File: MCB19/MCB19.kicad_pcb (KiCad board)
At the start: 2 copper layers, 204 x 81.5 mm, 99 parts, among them J401 USART, J402 DISABLE, J601 RJ45, J602 RJ45, J611 +BAT_IN, J612 -BAT_IN, J613 +BAT_OUT, J614 -BAT_OUT, Q601 IRFP260N, Q602 IRFP260N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

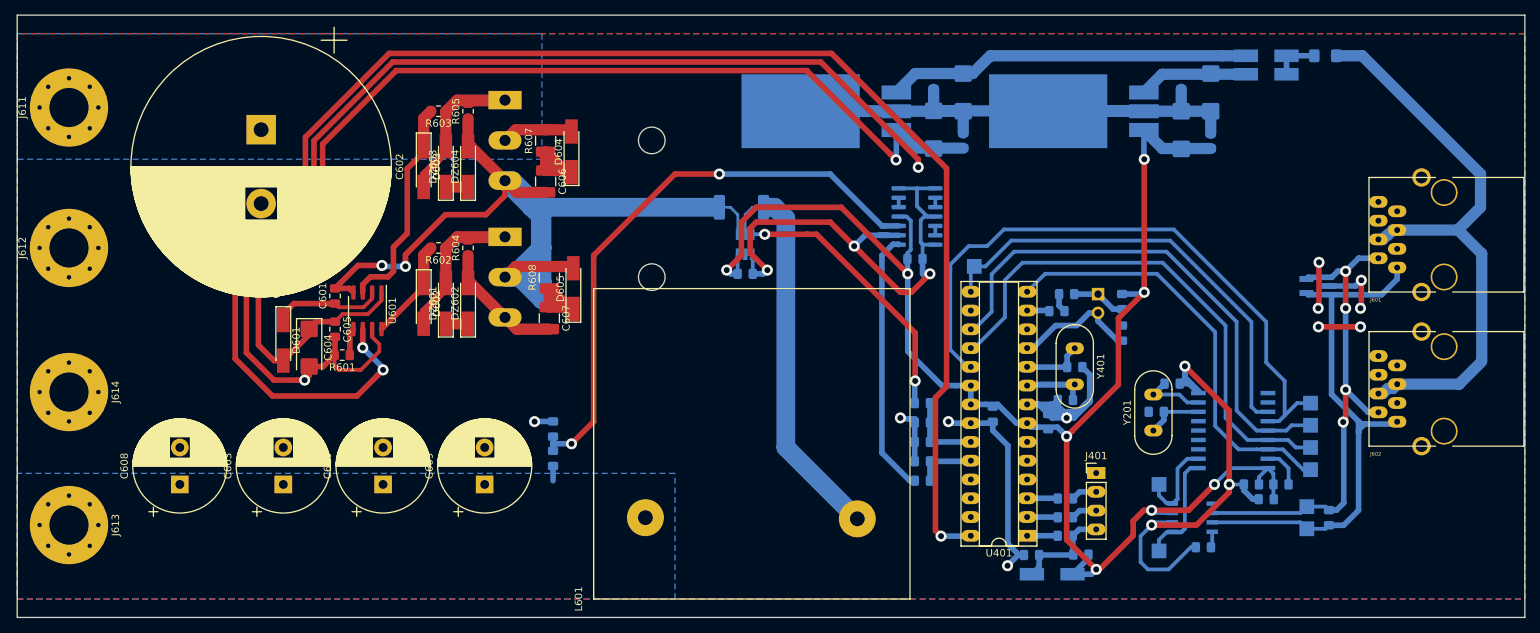
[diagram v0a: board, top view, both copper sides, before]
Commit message: trilhas aumentadas para 30mils
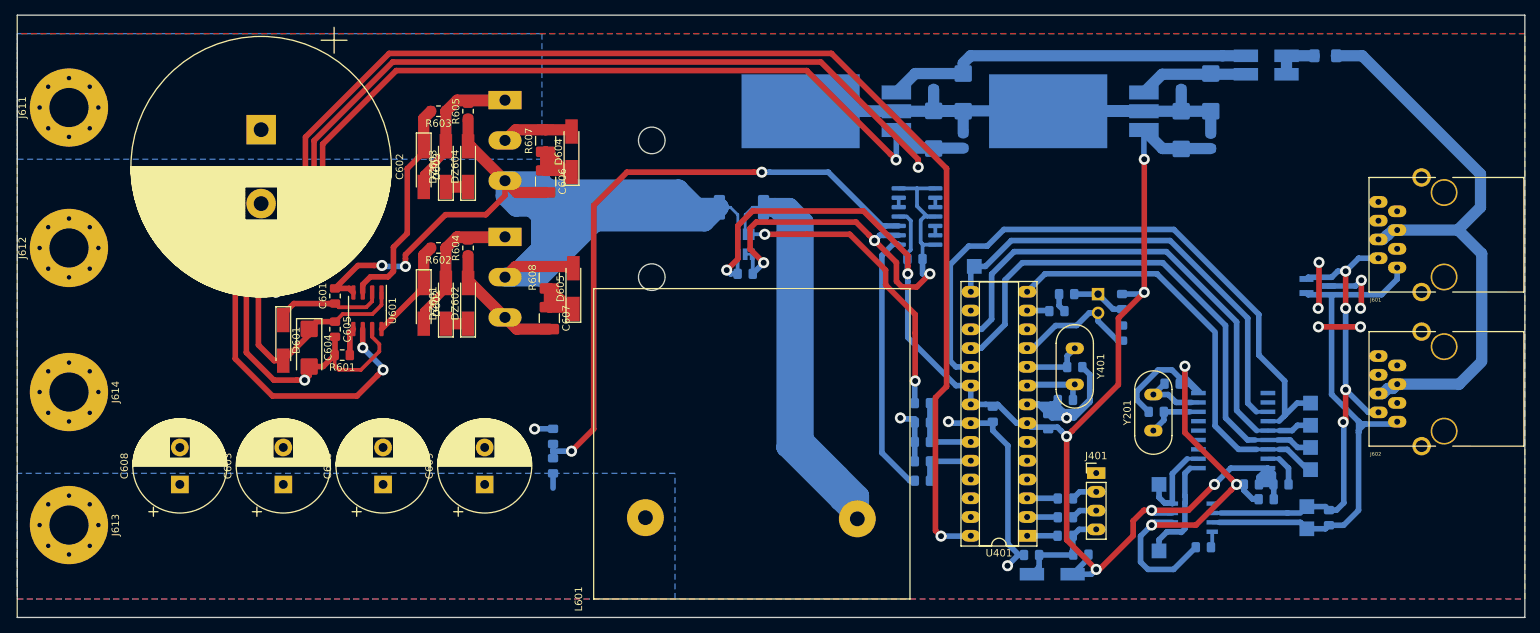
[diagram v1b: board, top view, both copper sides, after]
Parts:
- moved R609 1.00 mm to (122.5, 107.5)
- moved R610 1.00 mm to (122.5, 111.5)
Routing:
- net Net-(C601-Pad2): track 145.5 -> 238.5 mm
- net Net-(L601-Pad2): track 53.3 -> 124.5 mm
- net GND: track 545.9 -> 554.0 mm
- net +5V: track 212.2 -> 217.7 mm
- net Net-(R609-Pad2): track 82.2 -> 87.3 mm
- net /CANBUS/TXCAN: track 17.1 -> 21.7 mm
- net /MCU/INALLL: track 38.8 -> 41.4 mm
- net /SCK: track 86.3 -> 88.3 mm
- net Net-(C501-Pad1): track 49.4 -> 50.2 mm
- net /MOSI: track 70.7 -> 71.3 mm
- net /MISO: track 71.4 -> 71.9 mm

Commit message: 3D added
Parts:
- J402: moved to F.Cu
- moved J402 0.25 mm to (196.0, 88.2), turned to 0 degrees
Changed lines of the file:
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@@
     (visible_elements 7FFFFFFF)
     (pcbplotparams
-      (layerselection 0x00000_fffffffe)
+      (layerselection 0x3ffff_ffffffff)
       (usegerberextensions false)
       (usegerberattributes false)
@@
       (outputformat 4)
       (mirror false)
-      (drillshape 2)
+      (drillshape 0)
       (scaleselection 1)
-      (outputdirectory "GERBERS"))
+      (outputdirectory "PDF"))
   )
   (net 0 "")
@@
     (pad 3 thru_hole oval (at 10.9 0 270) (size 2.5 4.5) (drill 1.5) (layers *.Cu *.Mask)
       (net 37 "Net-(C601-Pad2)"))
-    (model ${KISYS3DMOD}/Package_TO_SOT_THT.3dshapes/TO-247-3_Horizontal_TabUp.wrl
-      (at (xyz 0 0 0))
+    (model "/home/joaoantoniocardoso/ZeniteSolar/2018/MCC18/Hardware/Shunt_sensor/Cuk_converter/KiCad/MCC_bibliotecas/MCCplaca.pretty/3D/User Library-TO-247H.step"
+      (offset (xyz 5.588 -19.558 3.048))
       (scale (xyz 1 1 1))
-      (rotate (xyz 0 0 0))
+      (rotate (xyz 90 0 0))
     )
   )
@@
     (pad 3 thru_hole oval (at 10.9 0 270) (size 2.5 4.5) (drill 1.5) (layers *.Cu *.Mask)
       (net 1 GND))
-    (model ${KISYS3DMOD}/Package_TO_SOT_THT.3dshapes/TO-247-3_Horizontal_TabUp.wrl
-      (at (xyz 0 0 0))
+    (model "/home/joaoantoniocardoso/ZeniteSolar/2018/MCC18/Hardware/Shunt_sensor/Cuk_converter/KiCad/MCC_bibliotecas/MCCplaca.pretty/3D/User Library-TO-247H.step"
+      (offset (xyz 5.588 -19.558 3.048))
       (scale (xyz 1 1 1))
-      (rotate (xyz 0 0 0))
+      (rotate (xyz 90 0 0))
     )
   )
@@
     )
   )
-  (module Connector_PinSocket_2.54mm:PinSocket_1x02_P2.54mm_Vertical (layer B.Cu)
-    (at 196.25 88.25 180)
+  (module Connector_PinSocket_2.54mm:PinSocket_1x02_P2.54mm_Vertical (layer F.Cu)
+    (at 196 88.25)
     (descr "Through hole straight socket strip, 1x02, 2.54mm pitch, single row (from Kicad 4.0.7), script generated")
     (tags "Through hole socket strip THT 1x02 2.54mm single row")
-    (fp_text reference J402 (at 0 2.77 180) (layer B.SilkS)
-      (effects (font (size 1 1) (thickness 0.15)) (justify mirror))
+    (fp_text reference J402 (at 0 -2.77 180) (layer F.SilkS)
+      (effects (font (size 1 1) (thickness 0.15)))
     )
-    (fp_text value DISABLE (at 0 -5.31 180) (layer B.Fab)
-      (effects (font (size 1 1) (thickness 0.15)) (justify mirror))
+    (fp_text value DISABLE (at 0 5.31 180) (layer F.Fab)
+      (effects (font (size 1 1) (thickness 0.15)))
     )
-    (fp_line (start -1.27 1.27) (end 0.635 1.27) (layer B.Fab) (width 0.1))
-    (fp_line (start 0.635 1.27) (end 1.27 0.635) (layer B.Fab) (width 0.1))
-    (fp_line (start 1.27 0.635) (end 1.27 -3.81) (layer B.Fab) (width 0.1))
-    (fp_line (start 1.27 -3.81) (end -1.27 -3.81) (layer B.Fab) (width 0.1))
-    (fp_line (start -1.27 -3.81) (end -1.27 1.27) (layer B.Fab) (width 0.1))
-    (fp_line (start -1.33 -1.27) (end 1.33 -1.27) (layer B.SilkS) (width 0.12))
-    (fp_line (start -1.33 -1.27) (end -1.33 -3.87) (layer B.SilkS) (width 0.12))
-    (fp_line (start -1.33 -3.87) (end 1.33 -3.87) (layer B.SilkS) (width 0.12))
-    (fp_line (start 1.33 -1.27) (end 1.33 -3.87) (layer B.SilkS) (width 0.12))
-    (fp_line (start 1.33 1.33) (end 1.33 0) (layer B.SilkS) (width 0.12))
-    (fp_line (start 0 1.33) (end 1.33 1.33) (layer B.SilkS) (width 0.12))
-    (fp_line (start -1.8 1.8) (end 1.75 1.8) (layer B.CrtYd) (width 0.05))
-    (fp_line (start 1.75 1.8) (end 1.75 -4.3) (layer B.CrtYd) (width 0.05))
-    (fp_line (start 1.75 -4.3) (end -1.8 -4.3) (layer B.CrtYd) (width 0.05))
-    (fp_line (start -1.8 -4.3) (end -1.8 1.8) (layer B.CrtYd) (width 0.05))
-    (fp_text user %R (at 0 -1.27 270) (layer B.Fab)
-      (effects (font (size 1 1) (thickness 0.15)) (justify mirror))
+    (fp_line (start -1.27 -1.27) (end 0.635 -1.27) (layer F.Fab) (width 0.1))
+    (fp_line (start 0.635 -1.27) (end 1.27 -0.635) (layer F.Fab) (width 0.1))
+    (fp_line (start 1.27 -0.635) (end 1.27 3.81) (layer F.Fab) (width 0.1))
+    (fp_line (start 1.27 3.81) (end -1.27 3.81) (layer F.Fab) (width 0.1))
+    (fp_line (start -1.27 3.81) (end -1.27 -1.27) (layer F.Fab) (width 0.1))
+    (fp_line (start -1.33 1.27) (end 1.33 1.27) (layer F.SilkS) (width 0.12))
+    (fp_line (start -1.33 1.27) (end -1.33 3.87) (layer F.SilkS) (width 0.12))
+    (fp_line (start -1.33 3.87) (end 1.33 3.87) (layer F.SilkS) (width 0.12))
+    (fp_line (start 1.33 1.27) (end 1.33 3.87) (layer F.SilkS) (width 0.12))
+    (fp_line (start 1.33 -1.33) (end 1.33 0) (layer F.SilkS) (width 0.12))
+    (fp_line (start 0 -1.33) (end 1.33 -1.33) (layer F.SilkS) (width 0.12))
+    (fp_line (start -1.8 -1.8) (end 1.75 -1.8) (layer F.CrtYd) (width 0.05))
+    (fp_line (start 1.75 -1.8) (end 1.75 4.3) (layer F.CrtYd) (width 0.05))
+    (fp_line (start 1.75 4.3) (end -1.8 4.3) (layer F.CrtYd) (width 0.05))
+    (fp_line (start -1.8 4.3) (end -1.8 -1.8) (layer F.CrtYd) (width 0.05))
+    (fp_text user %R (at 0 1.27 90) (layer F.Fab)
+      (effects (font (size 1 1) (thickness 0.15)))
     )
-    (pad 1 thru_hole rect (at 0 0 180) (size 1.7 1.7) (drill 1) (layers *.Cu *.Mask)
+    (pad 1 thru_hole rect (at 0 0) (size 1.7 1.7) (drill 1) (layers *.Cu *.Mask)
       (net 1 GND))
-    (pad 2 thru_hole oval (at 0 -2.54 180) (size 1.7 1.7) (drill 1) (layers *.Cu *.Mask)
+    (pad 2 thru_hole oval (at 0 2.54) (size 1.7 1.7) (drill 1) (layers *.Cu *.Mask)
       (net 29 "Net-(J402-Pad2)"))
     (model ${KISYS3DMOD}/Connector_PinSocket_2.54mm.3dshapes/PinSocket_1x02_P2.54mm_Vertical.wrl
@@
       (scale (xyz 1 1 1))
       (rotate (xyz 0 0 0))
+    )
+    (model ${KISYS3DMOD}/Package_DIP.3dshapes/DIP-28_W7.62mm.wrl
+      (offset (xyz 0 0 3.81))
+      (scale (xyz 1 1 1))
+      (rotate (xyz 0 0 0))
